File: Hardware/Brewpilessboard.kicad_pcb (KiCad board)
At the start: 2 copper layers, 94 x 91.8 mm, 15 parts, among them K1 2channelrelay, U1 ESP32_DevKit_V1_DOIT, U2 DS18B20, U3 DS18B20

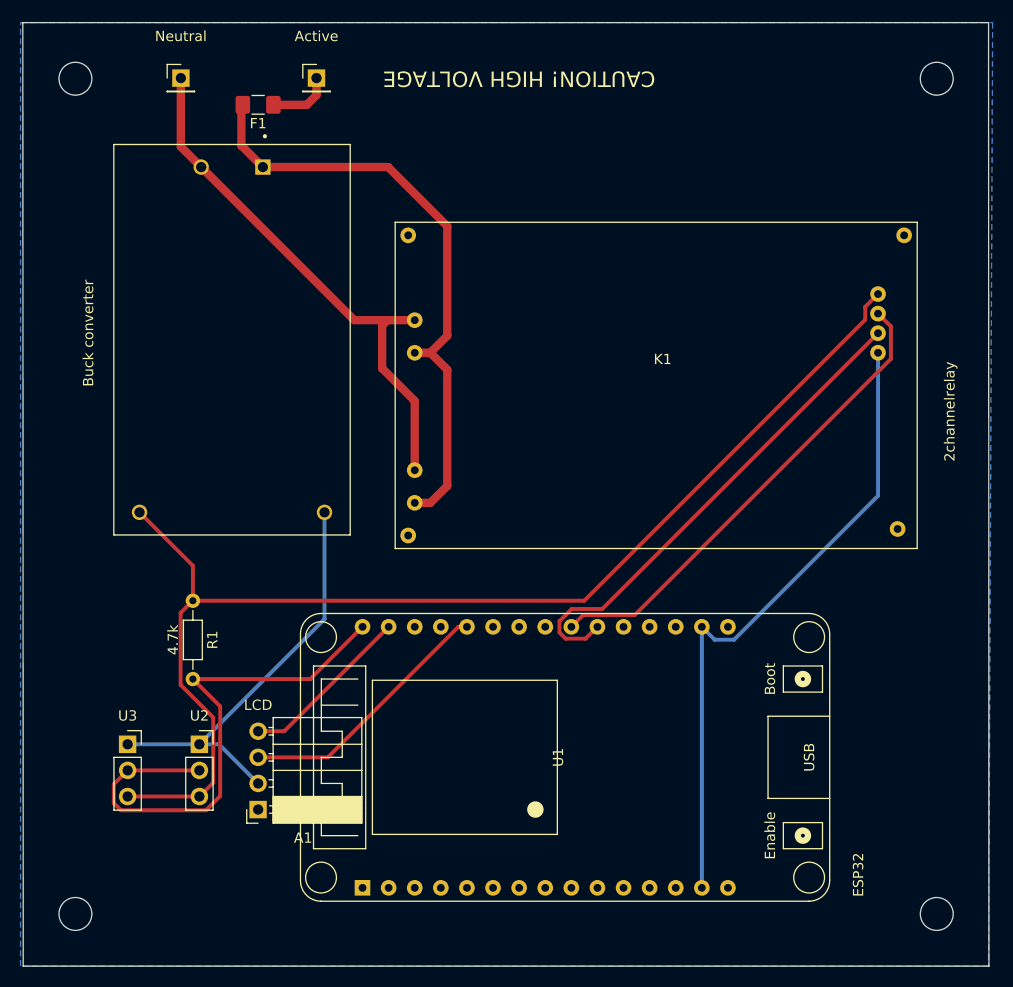
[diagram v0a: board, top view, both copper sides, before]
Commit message: Component orientation changed
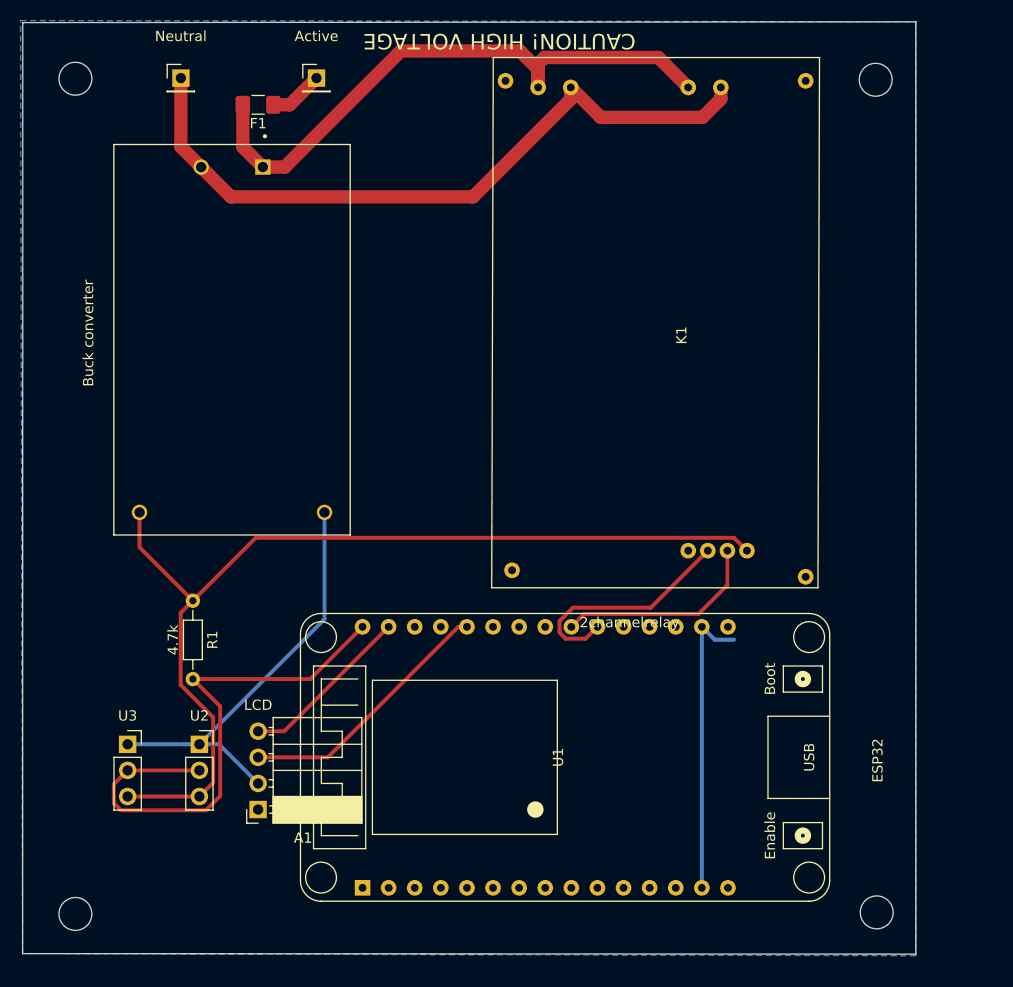
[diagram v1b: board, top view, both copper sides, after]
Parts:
- moved REF** 5.94 mm to (105.8, 23.0)
- moved REF** 5.84 mm to (105.9, 104.0)
- moved K1 5.51 mm to (84.4, 47.2), turned to 90 degrees
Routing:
- net GND: track 105.3 -> 71.6 mm
- net Net-(K1-Pad3): track 46.8 -> 20.2 mm
- net Net-(K1-Pad2): track 48.1 -> 22.8 mm
- net +5V: track 118.9 -> 96.1 mm
- net NEUT: track 52.6 -> 69.5 mm
- net Net-(F1-Pad1): track 6.10 -> 5.27 mm
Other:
- board size 94 x 91.8 mm -> 86.9 x 90.7 mm
- net class VAC: clearance 2 -> 1.5; trace_width 2 -> 1.5

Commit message: Minor silkscreen changes
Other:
- board text added: "Relay Board"
